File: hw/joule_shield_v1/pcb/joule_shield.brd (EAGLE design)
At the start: 60 x 40 mm, 143 parts, among them J1 MF-CON-MICROUSB-RIGHT, J4 USB_AUSB_A_SMT_RA, J5 JST-ZH5JST_ZH_SMT_VERT, J6 INTEL_JOULE_J6, J7 INTEL_JOULE_J7, J8 DM3ATDM3AT, Q1 NFETEMT3F, Q2 NFETEMT3F, Q3 NFETEMT3F, Q4 NFETEMT3F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

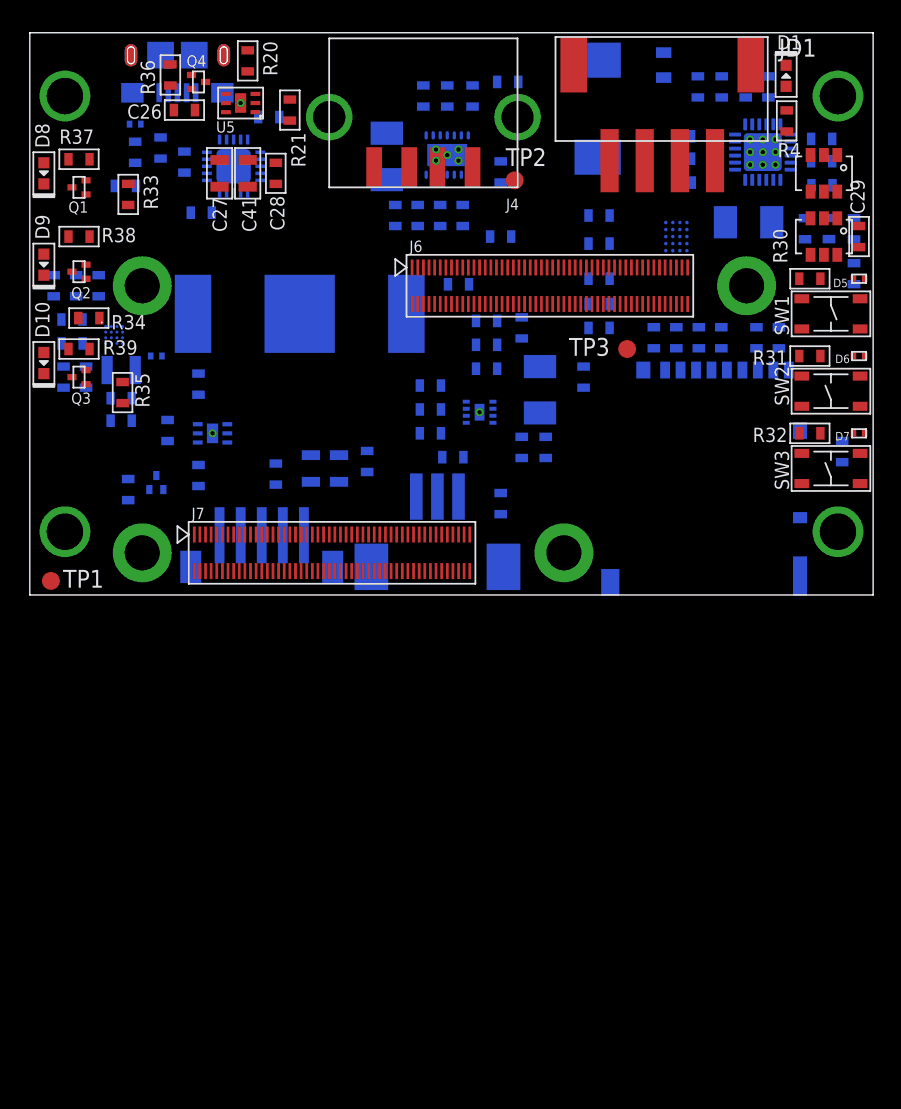
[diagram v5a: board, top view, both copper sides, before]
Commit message: joule shield: Made a pass at aligning all the parts.
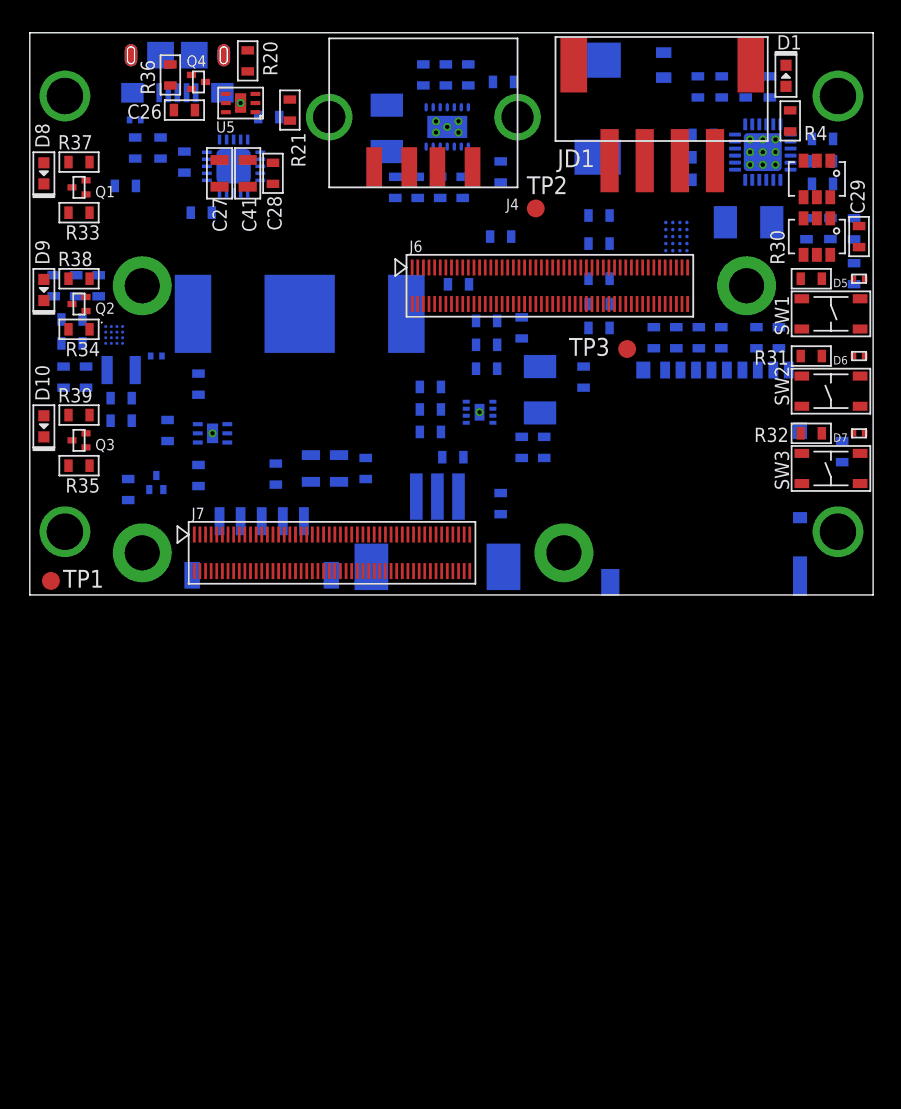
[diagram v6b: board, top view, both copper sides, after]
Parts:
- J5: value JST-ZH5JST_ZH_SMT_VERT -> JST-ZH5SMT_RA; device joule_shield:JST_ZH_SMT_VERT_5 -> joule_shield:JST_ZH_SMT_RA_5
- moved R35 6.05 mm to (3.50, 9.20), turned to 0 degrees
- moved R39 4.70 mm to (3.50, 12.8)
- moved D10 4.50 mm to (1.00, 12.0)
- moved Q3 4.50 mm to (3.50, 11.0)
- moved R33 3.73 mm to (3.50, 27.2), turned to 0 degrees
- moved R38 3.00 mm to (3.50, 22.5)
- moved TP2 2.50 mm to (36.0, 27.5)
- moved Q2 2.30 mm to (3.50, 20.7)
- moved L3 2.00 mm to (25.4, 33.2)
- moved C17 2.00 mm to (26.0, 29.0)
- moved C18 2.00 mm to (27.6, 29.0)
- moved C19 2.00 mm to (29.2, 29.0)
- moved C20 2.00 mm to (30.8, 29.0)
- moved U3 2.00 mm to (29.7, 33.3)
- moved D9 1.80 mm to (1.00, 21.7)
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
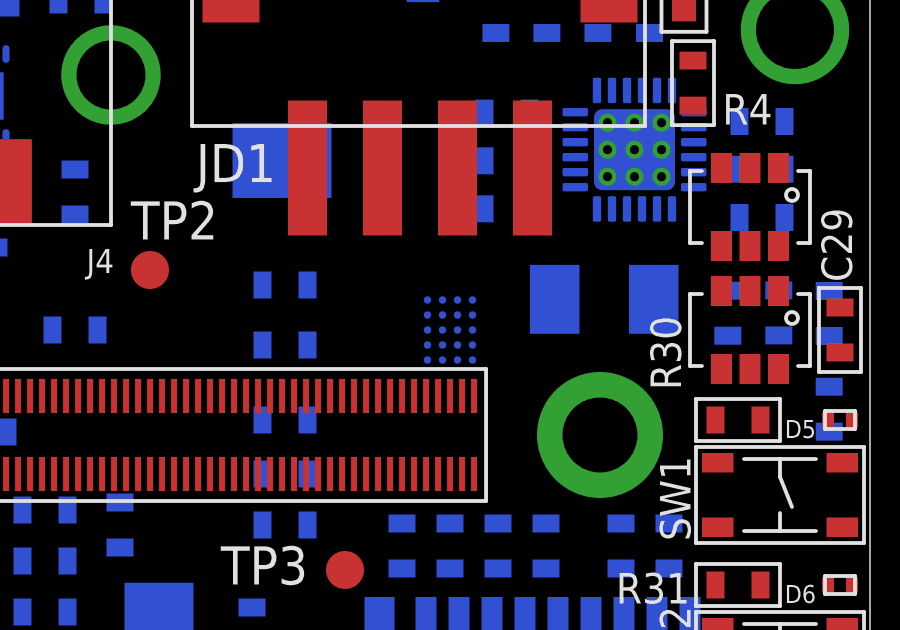
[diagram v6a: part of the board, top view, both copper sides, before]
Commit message: joule shield: Run ERC and connect up some wires which were inadvertently left unconnected.
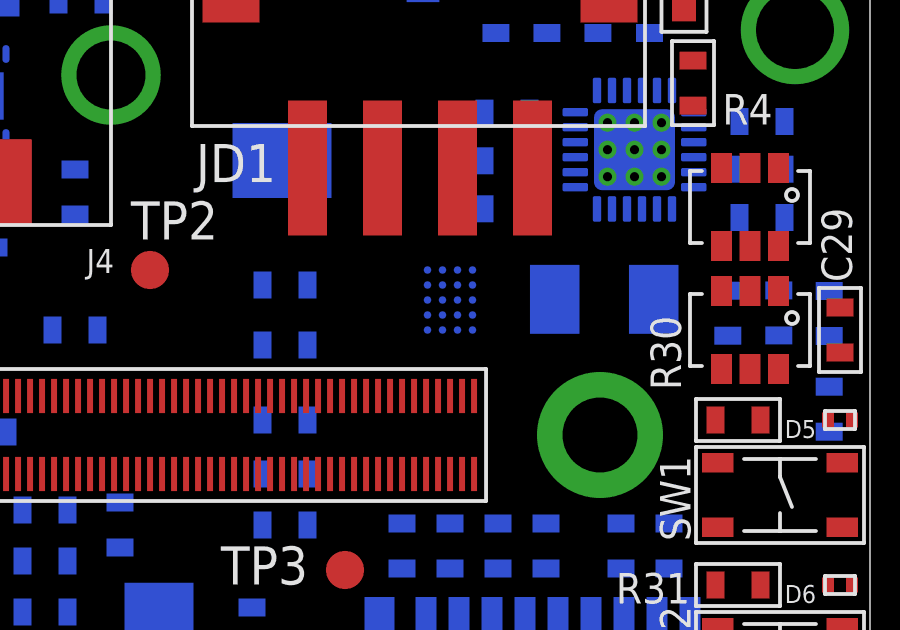
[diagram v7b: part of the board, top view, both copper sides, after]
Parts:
- moved U9 1.00 mm to (46.0, 26.5)
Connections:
- removed net SDCARD_PWR_DOWN_N: J6.91
- net I2C_0_SCL: now also J6.57
- net I2C_0_SDA: now also J6.95
- net JOULE_RX_18V: now also J6.26
- net JOULE_TX_18V: now also J6.28
- net VRTC: now also J6.11

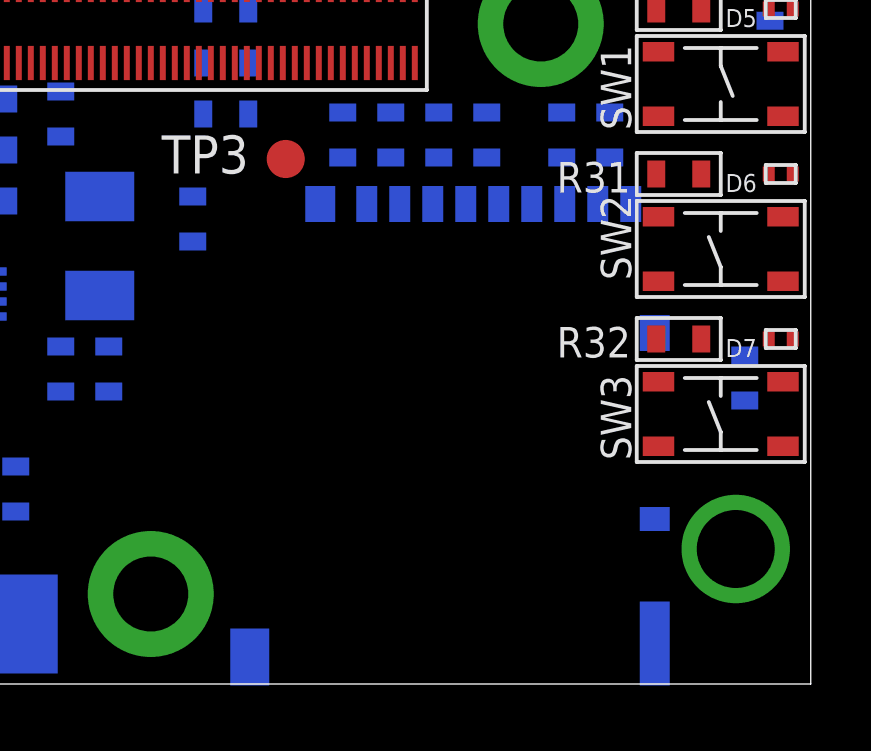
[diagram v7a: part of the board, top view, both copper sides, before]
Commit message: joule shield: Resolve some DRC errors.
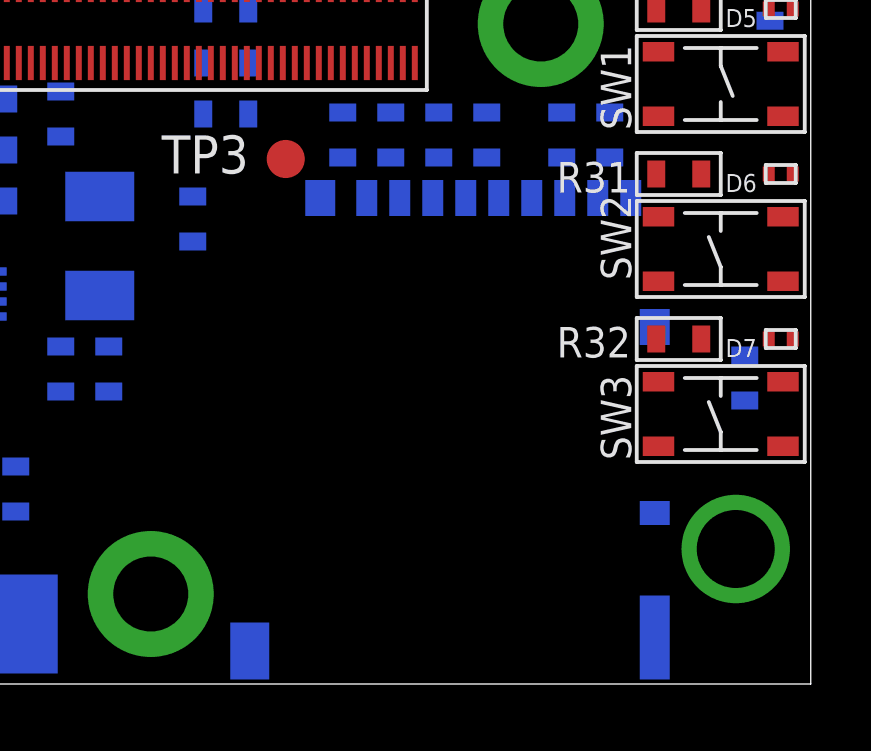
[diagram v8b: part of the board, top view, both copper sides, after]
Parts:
- moved J8 0.20 mm to (48.5, 16.2)
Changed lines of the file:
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@@
 <layers>
 <layer number="1" name="Top" color="4" fill="1" visible="yes" active="yes"/>
-<layer number="2" name="Route2" color="1" fill="3" visible="no" active="yes"/>
+<layer number="2" name="Route2" color="1" fill="3" visible="yes" active="yes"/>
 <layer number="3" name="Route3" color="4" fill="3" visible="no" active="no"/>
 <layer number="4" name="Route4" color="1" fill="4" visible="no" active="no"/>
@@
 <layer number="13" name="Route13" color="4" fill="5" visible="no" active="no"/>
 <layer number="14" name="Route14" color="1" fill="6" visible="no" active="no"/>
-<layer number="15" name="Route15" color="4" fill="6" visible="no" active="yes"/>
+<layer number="15" name="Route15" color="4" fill="6" visible="yes" active="yes"/>
 <layer number="16" name="Bottom" color="1" fill="1" visible="yes" active="yes"/>
 <layer number="17" name="Pads" color="2" fill="1" visible="yes" active="yes"/>
@@
 <attribute name="NAME" x="38.9" y="26.6" size="1.016" layer="26" font="vector" ratio="16" rot="MR0"/>
 </element>
-<element name="J8" library="joule_shield" package="DM3AT" value="DM3ATDM3AT" x="48.5" y="16" smashed="yes" rot="MR0">
-<attribute name="NAME" x="55.3" y="15.4" size="0.8" layer="22" rot="MR180"/>
+<element name="J8" library="joule_shield" package="DM3AT" value="DM3ATDM3AT" x="48.5" y="16.2" smashed="yes" rot="MR0">
+<attribute name="NAME" x="55.3" y="15.6" size="0.8" layer="22" rot="MR180"/>
 </element>
 <element name="C36" library="mf_passives" package="C0603" value="0.1uF" x="49.2" y="18.3" smashed="yes" rot="MR90">
@@
 <wire x1="9.8" y1="10.95" x2="11.95" y2="11.5" width="0" layer="19" extent="16-16"/>
 <wire x1="9.3" y1="38.405" x2="10" y2="36.25" width="0" layer="19" extent="1-16"/>
+<wire x1="7.2" y1="38.4" x2="9.3" y2="38.405" width="0" layer="19" extent="16-16"/>
 <wire x1="11.7" y1="38.405" x2="9.3" y2="38.405" width="0" layer="19" extent="16-16"/>
+<wire x1="13.8" y1="38.4" x2="11.7" y2="38.405" width="0" layer="19" extent="16-16"/>
 <wire x1="14.5" y1="32.4" x2="15" y2="35" width="0" layer="19" extent="1-16"/>
 <wire x1="15.5" y1="30.95" x2="14.5" y2="32.4" width="0" layer="19" extent="1-16"/>
@@
 <wire x1="46.802" y1="20.7" x2="46.402" y2="20.7" width="0" layer="19" extent="1-1"/>
 <wire x1="49.2" y1="19.05" x2="46.802" y2="20.7" width="0" layer="19" extent="1-16"/>
-<wire x1="50.7" y1="16" x2="49.2" y2="19.05" width="0" layer="19" extent="16-16"/>
-<wire x1="54" y1="16" x2="50.7" y2="16" width="0" layer="19" extent="16-16"/>
+<wire x1="50.7" y1="16.2" x2="49.2" y2="19.05" width="0" layer="19" extent="16-16"/>
+<wire x1="54" y1="16.2" x2="50.7" y2="16.2" width="0" layer="19" extent="16-16"/>
 <wire x1="8.5" y1="7.5" x2="9.8" y2="10.95" width="0" layer="19" extent="16-16"/>
 <wire x1="7" y1="8.25" x2="8.5" y2="7.5" width="0" layer="19" extent="16-16"/>
 <wire x1="58.6" y1="17" x2="59.075" y2="21.075" width="0" layer="19" extent="1-1"/>
 <wire x1="39.75" y1="27" x2="41.602" y2="23.3" width="0" layer="19" extent="1-16"/>
-<wire x1="54.8" y1="11.7" x2="54" y2="16" width="0" layer="19" extent="16-16"/>
-<wire x1="54.925" y1="7.925" x2="54.8" y2="11.7" width="0" layer="19" extent="1-16"/>
-<wire x1="58.6" y1="11.5" x2="54.8" y2="11.7" width="0" layer="19" extent="1-16"/>
+<wire x1="54.8" y1="11.9" x2="54" y2="16.2" width="0" layer="19" extent="16-16"/>
+<wire x1="54.925" y1="7.925" x2="54.8" y2="11.9" width="0" layer="19" extent="1-16"/>
+<wire x1="58.6" y1="11.5" x2="54.8" y2="11.9" width="0" layer="19" extent="1-16"/>
 <wire x1="35" y1="9.75" x2="32" y2="13" width="0" layer="19" extent="16-16"/>
 <wire x1="36.6" y1="9.75" x2="35" y2="9.75" width="0" layer="19" extent="16-16"/>
@@
 <wire x1="2.75" y1="27.2" x2="4" y2="29.5" width="0" layer="19" extent="1-1"/>
 <wire x1="19.2" y1="20" x2="27.602" y2="20.7" width="0" layer="19" extent="1-16"/>
-<wire x1="13.8" y1="38.4" x2="11.7" y2="38.405" width="0" layer="19" extent="16-16"/>
-<wire x1="7.2" y1="38.4" x2="9.3" y2="38.405" width="0" layer="19" extent="16-16"/>
 </signal>
 <signal name="N$2">
@@
 <contactref element="R44" pad="P$2"/>
 <wire x1="53.3" y1="17.55" x2="46.75" y2="27.5" width="0" layer="19" extent="16-16"/>
-<wire x1="52.9" y1="16" x2="53.3" y2="17.55" width="0" layer="19" extent="16-16"/>
+<wire x1="52.9" y1="16.2" x2="53.3" y2="17.55" width="0" layer="19" extent="16-16"/>
 </signal>
 <signal name="N$42">
@@
 <contactref element="R43" pad="P$2"/>
 <wire x1="44.4" y1="17.55" x2="46.25" y2="26" width="0" layer="19" extent="16-16"/>
-<wire x1="45.2" y1="16" x2="44.4" y2="17.55" width="0" layer="19" extent="16-16"/>
+<wire x1="45.2" y1="16.2" x2="44.4" y2="17.55" width="0" layer="19" extent="16-16"/>
 </signal>
 <signal name="N$43">
@@
 <contactref element="R42" pad="P$2"/>
 <wire x1="46" y1="17.55" x2="46.75" y2="26" width="0" layer="19" extent="16-16"/>
-<wire x1="46.3" y1="16" x2="46" y2="17.55" width="0" layer="19" extent="16-16"/>
+<wire x1="46.3" y1="16.2" x2="46" y2="17.55" width="0" layer="19" extent="16-16"/>
 </signal>
 <signal name="N$44">
@@
 <contactref element="R41" pad="P$2"/>
 <wire x1="47.6" y1="17.55" x2="46.25" y2="27" width="0" layer="19" extent="16-16"/>
-<wire x1="47.4" y1="16" x2="47.6" y2="17.55" width="0" layer="19" extent="16-16"/>
+<wire x1="47.4" y1="16.2" x2="47.6" y2="17.55" width="0" layer="19" extent="16-16"/>
 </signal>
 <signal name="N$45">
 <contactref element="J8" pad="5"/>
 <contactref element="U9" pad="D3"/>
-<wire x1="49.6" y1="16" x2="46.75" y2="26.5" width="0" layer="19" extent="16-16"/>
+<wire x1="49.6" y1="16.2" x2="46.75" y2="26.5" width="0" layer="19" extent="16-16"/>
 </signal>
 <signal name="SDCARD_CD">
@@
 <contactref element="R26" pad="P$2"/>
 <wire x1="57.8" y1="9.45" x2="42.802" y2="23.3" width="0" layer="19" extent="1-16"/>
-<wire x1="54.8" y1="5.5" x2="57.8" y2="9.45" width="0" layer="19" extent="16-16"/>
+<wire x1="54.8" y1="5.7" x2="57.8" y2="9.45" width="0" layer="19" extent="16-16"/>
 </signal>
 <signal name="SDCARD_D0">
@@
 <wire x1="47.6" y1="19.05" x2="46" y2="19.05" width="0" layer="19" extent="16-16"/>
 <wire x1="49.2" y1="17.55" x2="47.6" y2="19.05" width="0" layer="19" extent="16-16"/>
-<wire x1="48.5" y1="16" x2="49.2" y2="17.55" width="0" layer="19" extent="16-16"/>
+<wire x1="48.5" y1="16.2" x2="49.2" y2="17.55" width="0" layer="19" extent="16-16"/>
 <wire x1="51.7" y1="19.05" x2="49.2" y2="17.55" width="0" layer="19" extent="16-16"/>
 <wire x1="53.3" y1="19.05" x2="51.7" y2="19.05" width="0" layer="19" extent="16-16"/>
@@
 <contactref element="R45" pad="P$2"/>
 <wire x1="51.7" y1="17.55" x2="46.75" y2="27" width="0" layer="19" extent="16-16"/>
-<wire x1="51.8" y1="16" x2="51.7" y2="17.55" width="0" layer="19" extent="16-16"/>
+<wire x1="51.8" y1="16.2" x2="51.7" y2="17.55" width="0" layer="19" extent="16-16"/>
 </signal>
 <signal name="ISH_GPIO_4">
